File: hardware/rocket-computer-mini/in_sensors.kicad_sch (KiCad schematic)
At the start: 22 parts, among them J1 BM05B-SRSS-TB, J8 CON-SMA-EDGE-S, U16 E220-900MM22S, U2 ISM6HG256XTR, U27 TPS22810DRVR, U3 IIS2MDCTR, U4 BMP585, U5 LC86GLAMD

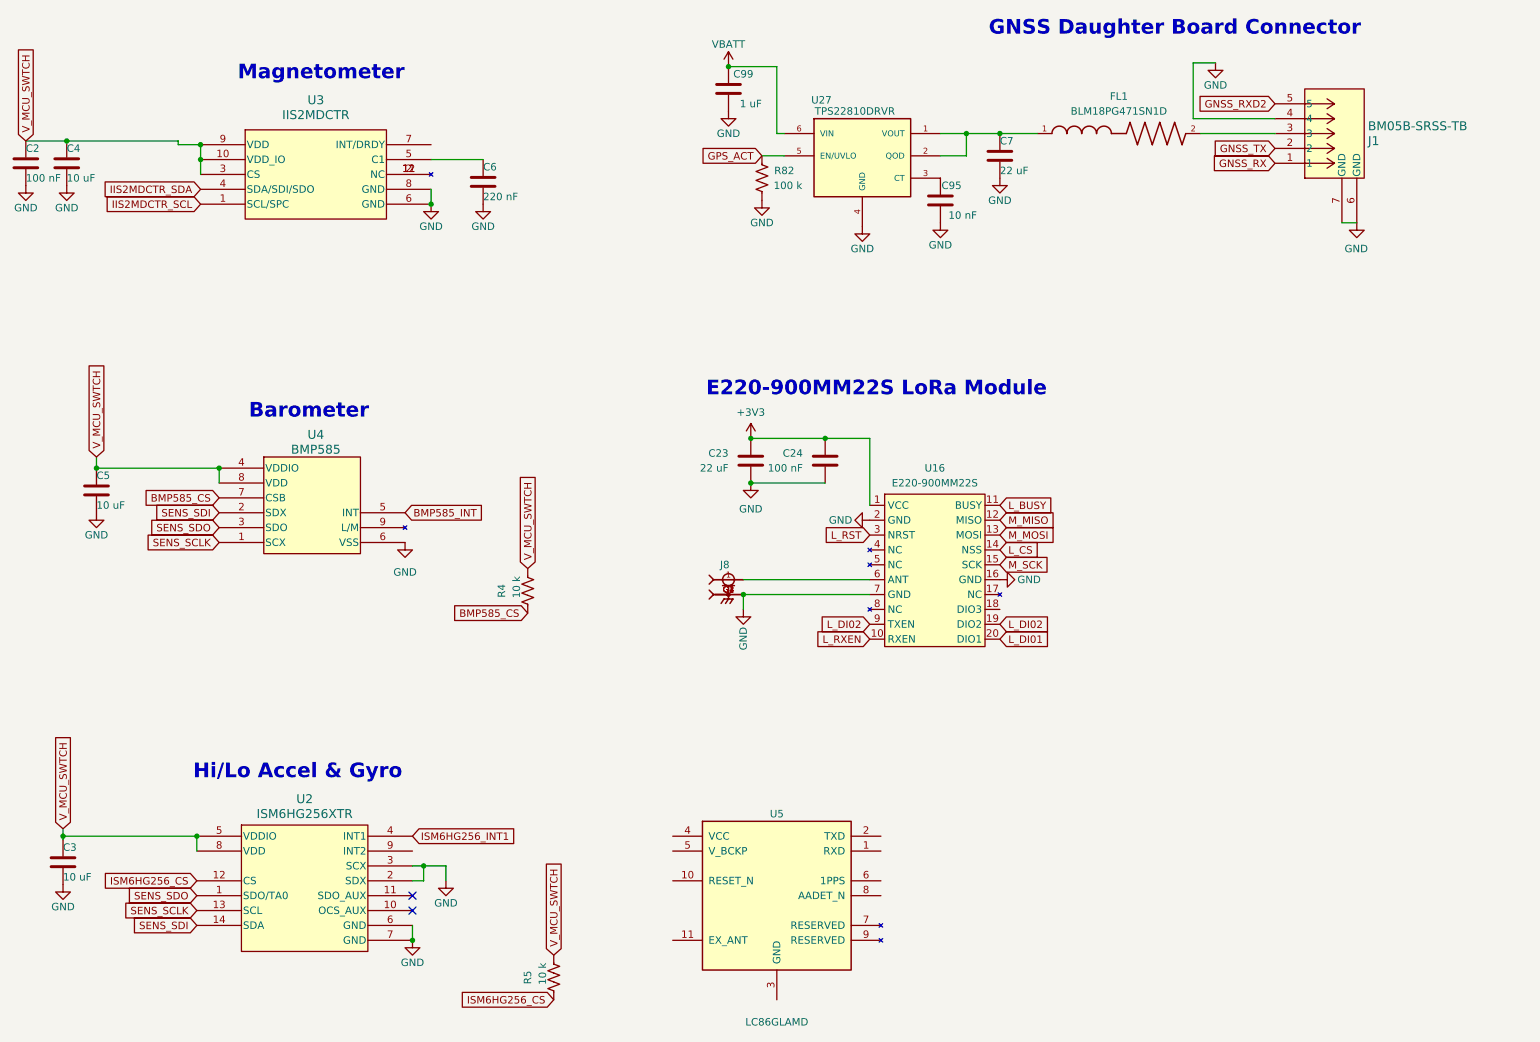
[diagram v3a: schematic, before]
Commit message: hardware: move two signals off the risky processor pads
Audits every special-function pin the assignment touches and moves the two that
were not defensible, using pads freed by dropping power-good and the peripheral
enable.

BMP585_INT leaves GPIO26 for GPIO41. GPIO26 is the quad PSRAM chip select, and
the evidence that this part has no PSRAM only covers the octal variety -- the V7
board drove GPIO34-38 on hardware that was built and flown, which rules out
octal but says nothing about quad, and quad uses exactly GPIO26. Rather than
resolve the package suffix, the pin is now simply unused.

PYRO4_CONT leaves GPIO44 for GPIO42, returning the full serial console. A
console that works from first power-on with no adapter is worth more during
bring-up than the JTAG pads it costs.

Everything else checks out. GPIO27-32 carry the external boot flash and are used
as intended. GPIO33-37 and GPIO47/48 serve octal PSRAM only, which the V7
hardware proves is absent. GPIO39-42 are ordinary GPIO once debug is given up.
GPIO3 drives a switch enable and its pulldown holds it low through reset, which
is the behaviour that pad wants anyway.

GPIO45 stays unused on purpose: it sets the flash rail voltage at reset, and any
signal whose boot level the design does not control can stop the board booting.

Four pads now free -- GPIO26, GPIO43, GPIO44, GPIO45 -- and both hazardous ones
are among them. Schematic only.

Co-Authored-By: Claude Opus 5 <noreply@anthropic.com>
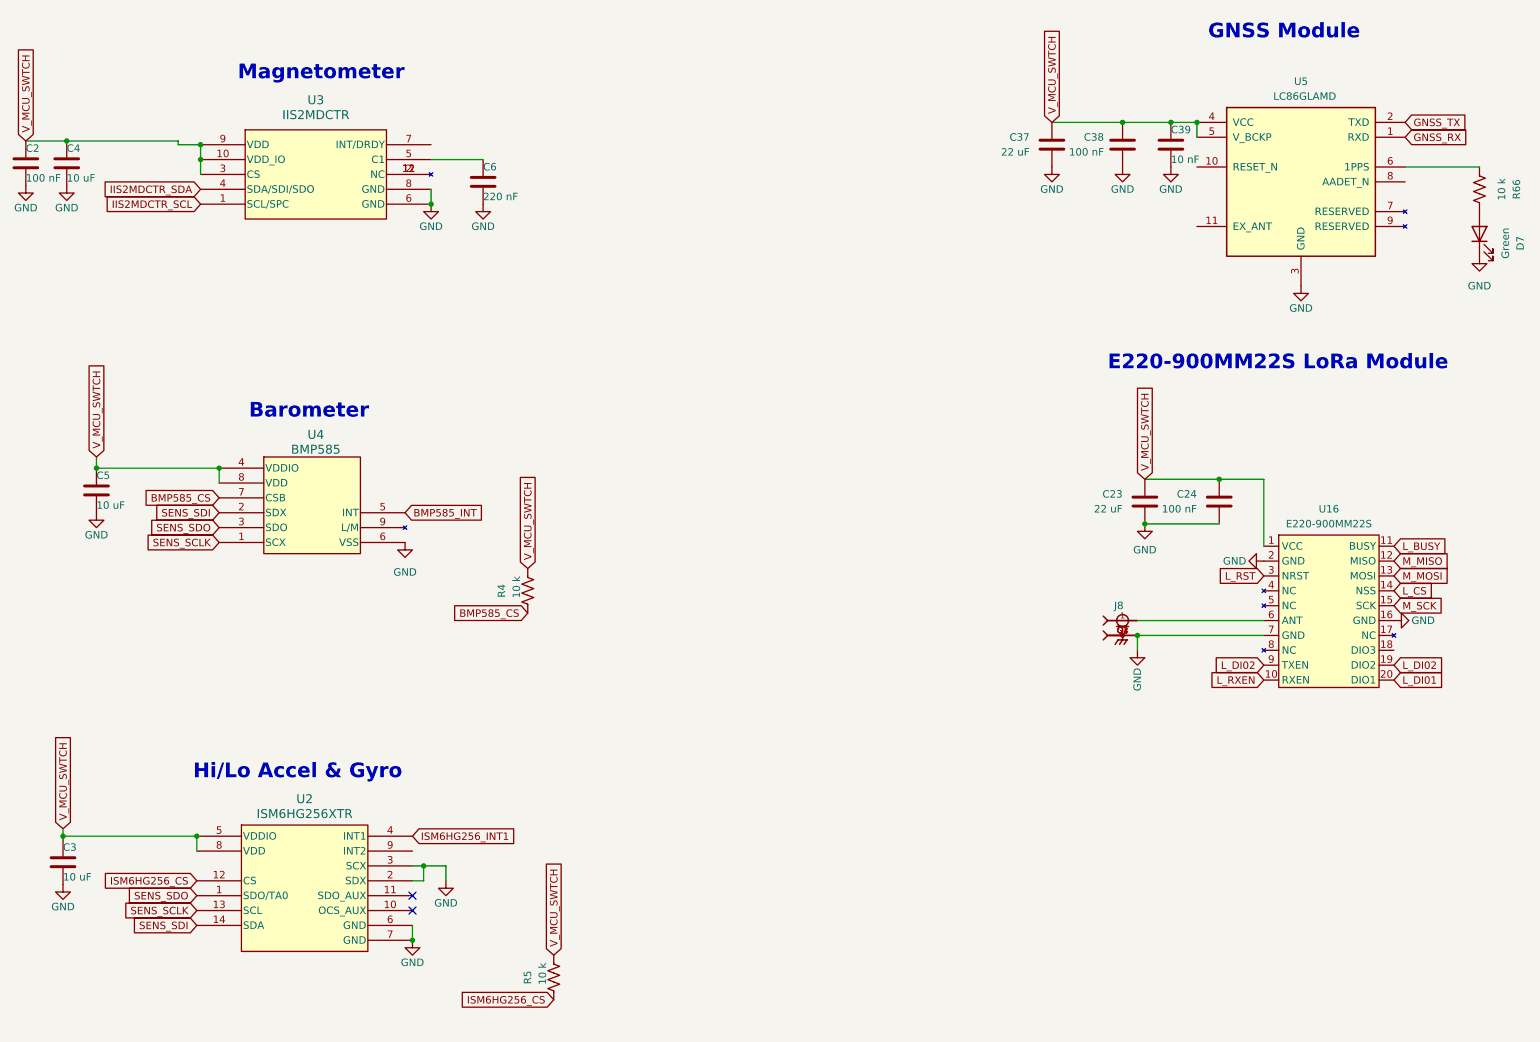
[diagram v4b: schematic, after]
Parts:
- removed C7: 22 uF, Capacitor_SMD:C_0805_2012Metric, symbol Device:C
- removed C95: 10 nF, Capacitor_SMD:C_0402_1005Metric, symbol Device:C
- removed C99: 1 uF, Capacitor_SMD:C_0402_1005Metric, symbol Device:C
- removed FL1: BLM18PG471SN1D, Footprints:BEADC1608X95N, symbol Custom:BLM18PG471SN1D
- removed J1: BM05B-SRSS-TB, Footprints:CONN_BM05B-SRSS-TB_JST, symbol Custom:BM05B-SRSS-TB
- removed R82: 100 k, Resistor_SMD:R_0402_1005Metric, symbol Device:R_US
- removed U27: TPS22810DRVR, Footprints:SON65P200X200X80-7N, symbol Custom:TPS22810DRVR
- added C37: 22 uF, Capacitor_SMD:C_0805_2012Metric, symbol Device:C
- added C38: 100 nF, Capacitor_SMD:C_0402_1005Metric, symbol Device:C
- added C39: 10 nF, Capacitor_SMD:C_0402_1005Metric, symbol Device:C
- added D7: Green, LED_SMD:LED_0402_1005Metric, symbol Device:LED
- added R66: 10 k, Resistor_SMD:R_0402_1005Metric, symbol Device:R_US
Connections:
- net +3V3 is gone; now on net V_MCU_SWTCH: C23.2, C24.2, U16.1 (VCC)
- net GND: now also C37.1, C38.1, C39.2, D7.1 (K)
- net GNSS_RX: now also U5.1 (RXD)
- net GNSS_TX: now also U5.2 (TXD)
- net V_MCU_SWTCH: now also U5.4 (VCC), U5.5 (V_BCKP), C37.2, C38.2, C39.1
- net at U5.6 (1PPS): now also R66.1
- new net: D7.2 (A), R66.2
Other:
- note added: "GNSS Module"
- note removed: "GNSS Daughter Board Connector"
- moved on the sheet: C23, C24, J8, U16, U5

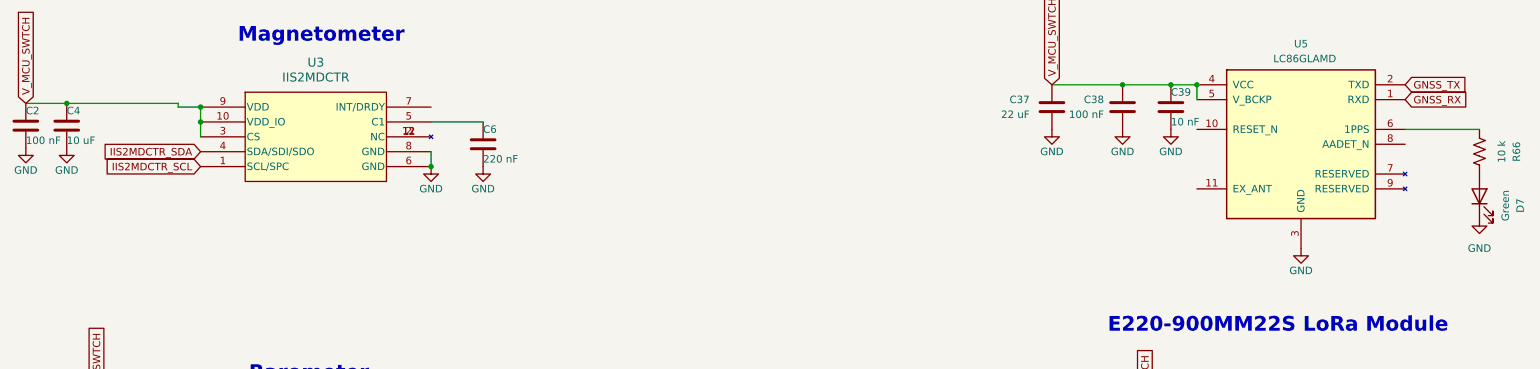
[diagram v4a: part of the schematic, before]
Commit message: hardware: magnetometer onto the shared I2C bus, NAND to the switched rail, radio RX-enable wired
Three connectivity fixes and one bus correction.

The magnetometer joins the power monitor on one I2C bus, renamed SEN_SCL /
SEN_SDA, with both parts and the processor on it. The rename initially stranded
the bus pull-ups on the old net names, leaving an open-drain bus with nothing to
pull it high and both devices unusable; R67 and R69 are now back on the live
nets.

The NAND moves to the switched rail. That closes the split introduced when the
radio moved to switched power while the NAND stayed always-on -- a powered
device driving a bus into unpowered silicon. Both bus slaves now share one
domain and the only always-on device is the processor, whose pins are inputs
after reset (datasheet Table 2-1), so nothing drives into a dead rail. The cost
is that the log memory now drops out whenever the peripheral rail is cycled, and
NAND can lose a block if power goes during program or erase -- firmware should
close the log before any deliberate cycle.

The radio's receive-enable reaches GPIO44. This matches what both existing radio
boards do rather than the inverter previously suggested here: the vendor's split
shorts DIO2 to TXEN on the board and brings only the RX half to a processor pin.
DIO3 stays floating, as it must -- the module has its own passive crystal and
must never be configured for a DIO3-powered TCXO.

Firmware already carries rxen_pin in the radio config and both the daughterboard
and base-station projects set it, but the out-computer project defines no
LORA_RXEN_PIN, so this pin does nothing until the board map declares it. The
base-station sources record this same defect having shipped once already --
"was defined but never driven, RXEN floated in RX".

Two pads remain: GPIO26, which the in-package PSRAM owns and cannot be used, and
GPIO43, kept free so the boot ROM can still print. ERC 637 -> 629.

Co-Authored-By: Claude Opus 5 <noreply@anthropic.com>
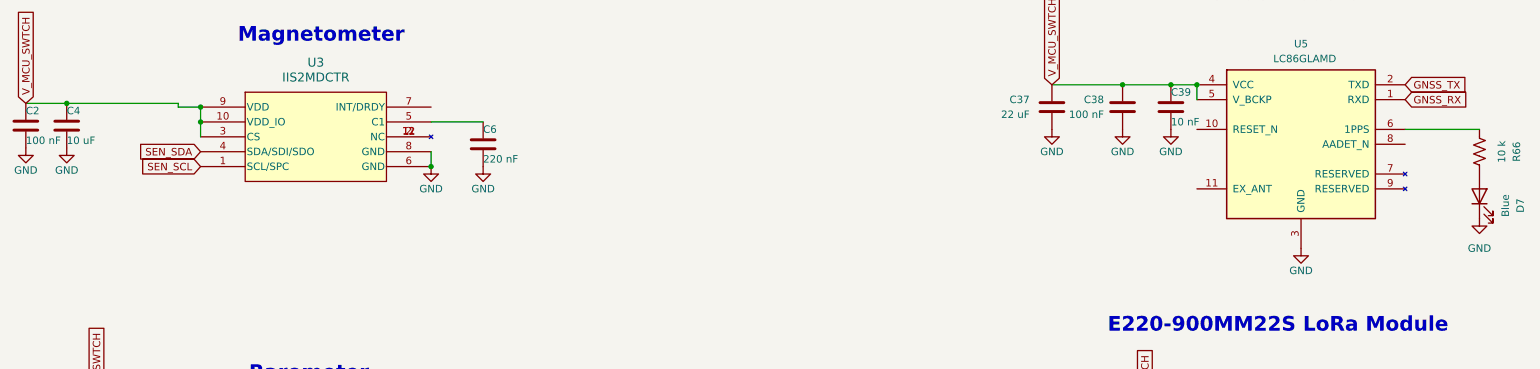
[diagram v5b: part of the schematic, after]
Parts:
- D7: value Green -> Blue
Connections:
- net IIS2MDCTR_SCL renamed SEN_SCL
- net IIS2MDCTR_SDA renamed SEN_SDA
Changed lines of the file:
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@@
 		)
 	)
-	(global_label "IIS2MDCTR_SDA"
+	(global_label "BMP585_CS"
+		(shape input)
+		(at 49.53 102.235 180)
+		(fields_autoplaced yes)
+		(effects
+			(font
+				(size 1.27 1.27)
+			)
+			(justify right)
+		)
+		(property "Intersheetrefs" "${INTERSHEET_REFS}"
+			(at 35.4778 102.235 0)
+			(hide yes)
+			(show_name no)
+			(do_not_autoplace no)
+			(effects
+				(font
+					(size 1.27 1.27)
+				)
+				(justify right)
+			)
+		)
+	)
+	(global_label "L_BUSY"
+		(shape input)
+		(at 250.19 110.49 0)
+		(fields_autoplaced yes)
+		(effects
+			(font
+				(size 1.27 1.27)
+			)
+			(justify left)
+		)
+		(property "Intersheetrefs" "${INTERSHEET_REFS}"
+			(at 259.4974 110.4106 0)
+			(hide yes)
+			(show_name no)
+			(do_not_autoplace no)
+			(effects
+				(font
+					(size 1.27 1.27)
+				)
+				(justify left)
+			)
+		)
+	)
+	(global_label "SEN_SCL"
+		(shape input)
+		(at 46.355 52.07 180)
+		(fields_autoplaced yes)
+		(effects
+			(font
+				(size 1.27 1.27)
+			)
+			(justify right)
+		)
+		(property "Intersheetrefs" "${INTERSHEET_REFS}"
+			(at 35.2056 52.07 0)
+			(hide yes)
+			(show_name no)
+			(do_not_autoplace no)
+			(effects
+				(font
+					(size 1.27 1.27)
+				)
+				(justify right)
+			)
+		)
+	)
+	(global_label "GNSS_RX"
+		(shape input)
+		(at 252.095 40.64 0)
+		(fields_autoplaced yes)
+		(effects
+			(font
+				(size 1.27 1.27)
+			)
+			(justify left)
+		)
+		(property "Intersheetrefs" "${INTERSHEET_REFS}"
+			(at 263.5468 40.64 0)
+			(hide yes)
+			(show_name no)
+			(do_not_autoplace no)
+			(effects
+				(font
+					(size 1.27 1.27)
+				)
+				(justify left)
+			)
+		)
+	)
+	(global_label "SEN_SDA"
 		(shape input)
 		(at 46.355 49.53 180)
@@
 		)
 		(property "Intersheetrefs" "${INTERSHEET_REFS}"
-			(at 28.9765 49.53 0)
+			(at 35.1451 49.53 0)
 			(hide yes)
 			(show_name no)
@@
 		)
 	)
-	(global_label "BMP585_CS"
-		(shape input)
-		(at 49.53 102.235 180)
-		(fields_autoplaced yes)
-		(effects
-			(font
-				(size 1.27 1.27)
-			)
-			(justify right)
-		)
-		(property "Intersheetrefs" "${INTERSHEET_REFS}"
-			(at 35.4778 102.235 0)
-			(hide yes)
-			(show_name no)
-			(do_not_autoplace no)
-			(effects
-				(font
-					(size 1.27 1.27)
-				)
-				(justify right)
-			)
-		)
-	)
-	(global_label "L_BUSY"
-		(shape input)
-		(at 250.19 110.49 0)
+	(global_label "V_MCU_SWTCH"
+		(shape input)
+		(at 191.77 38.1 90)
 		(fields_autoplaced yes)
 		(effects
@@
 		)
 		(property "Intersheetrefs" "${INTERSHEET_REFS}"
-			(at 259.4974 110.4106 0)
-			(hide yes)
-			(show_name no)
-			(do_not_autoplace no)
-			(effects
-				(font
-					(size 1.27 1.27)
-				)
-				(justify left)
-			)
-		)
-	)
-	(global_label "GNSS_RX"
-		(shape input)
-		(at 252.095 40.64 0)
+			(at 191.77 21.8101 90)
+			(hide yes)
+			(show_name no)
+			(do_not_autoplace no)
+			(effects
+				(font
+					(size 1.27 1.27)
+				)
+				(justify left)
+			)
+		)
+	)
+	(global_label "V_MCU_SWTCH"
+		(shape input)
+		(at 16.51 41.275 90)
 		(fields_autoplaced yes)
 		(effects
@@
 		)
 		(property "Intersheetrefs" "${INTERSHEET_REFS}"
-			(at 263.5468 40.64 0)
-			(hide yes)
-			(show_name no)
-			(do_not_autoplace no)
-			(effects
-				(font
-					(size 1.27 1.27)
-				)
-				(justify left)
-			)
-		)
-	)
-	(global_label "V_MCU_SWTCH"
-		(shape input)
-		(at 191.77 38.1 90)
-		(fields_autoplaced yes)
-		(effects
-			(font
-				(size 1.27 1.27)
-			)
-			(justify left)
-		)
-		(property "Intersheetrefs" "${INTERSHEET_REFS}"
-			(at 191.77 21.8101 90)
-			(hide yes)
-			(show_name no)
-			(do_not_autoplace no)
-			(effects
-				(font
-					(size 1.27 1.27)
-				)
-				(justify left)
-			)
-		)
-	)
-	(global_label "V_MCU_SWTCH"
-		(shape input)
-		(at 16.51 41.275 90)
-		(fields_autoplaced yes)
-		(effects
-			(font
-				(size 1.27 1.27)
-			)
-			(justify left)
-		)
-		(property "Intersheetrefs" "${INTERSHEET_REFS}"
 			(at 16.51 24.9851 90)
 			(hide yes)
@@
 				)
 				(justify left)
-			)
-		)
-	)
-	(global_label "IIS2MDCTR_SCL"
-		(shape input)
-		(at 46.355 52.07 180)
-		(fields_autoplaced yes)
-		(effects
-			(font
-				(size 1.27 1.27)
-			)
-			(justify right)
-		)
-		(property "Intersheetrefs" "${INTERSHEET_REFS}"
-			(at 29.037 52.07 0)
-			(hide yes)
-			(show_name no)
-			(do_not_autoplace no)
-			(effects
-				(font
-					(size 1.27 1.27)
-				)
-				(justify right)
 			)
 		)
@@
 			)
 		)
-		(property "Value" "Green"
+		(property "Value" "Blue"
 			(at 269.24 58.7375 0)
 			(show_name no)
